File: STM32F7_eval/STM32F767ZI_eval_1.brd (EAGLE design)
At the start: 76.2 x 53.3 mm, 100 parts, among them CN3 GROVE-4P-CONN-I2C-90D, CN4 GROVE-4P-CONN-AN01-90D, CN5 ARDUINO_COMPAT_IF, CN6 STLINKV21_SWD_IF, CN7 WFT0750CZ09-SMD_, CN8 MCO_IF, CN9 UART_IF, Q1 PMF370XN_, SW1 SKRPACE010_, SW2 SKRPACE010_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

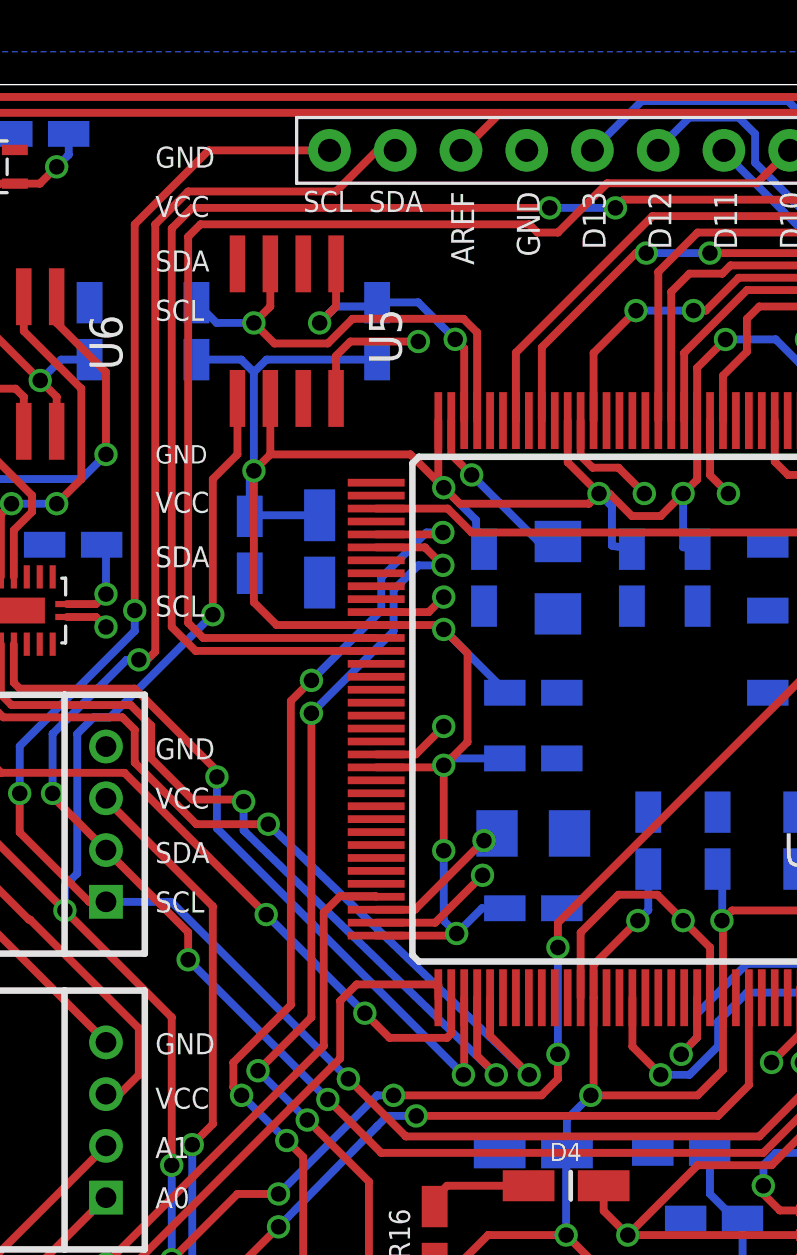
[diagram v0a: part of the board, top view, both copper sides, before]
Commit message: 評価回路を修正
・オプションデバイス電圧とメイン電圧間にジャンパーを挿入
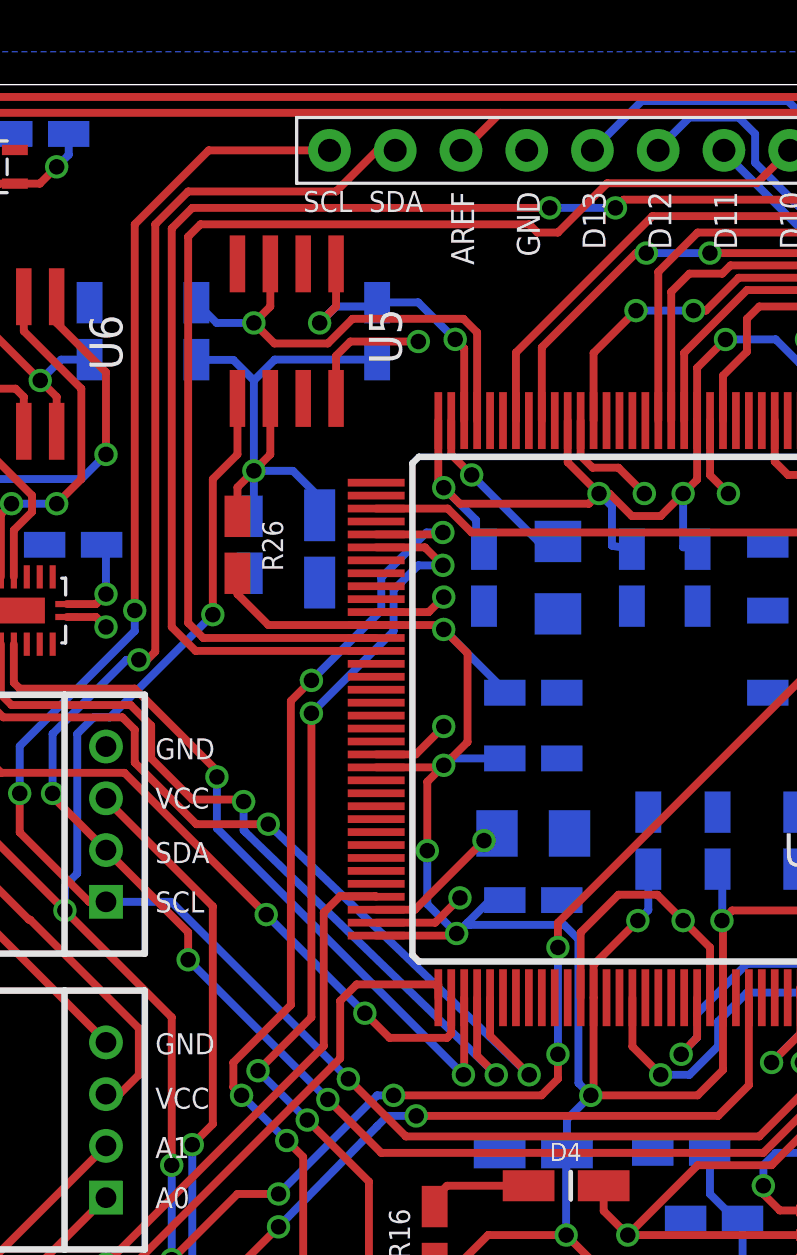
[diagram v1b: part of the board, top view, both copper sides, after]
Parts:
- added R26: 0, Parts:SMD_1608_DEV
- moved C4 0.32 mm to (26.7, 21.8)
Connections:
- new net VCC_STSAFE: C28.1, C29.1, R19.2, R20.2, R26.1, U5.2
- net VDD: now also R26.2; no longer C28.1, C29.1, R19.2, R20.2, U5.2
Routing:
- net VCC_STSAFE: track 0.00 -> 22.1 mm, vias 0 -> 1
- net VDD: track 290.2 -> 272.8 mm, vias 25 -> 24
- net 0V: track 185.7 -> 184.4 mm

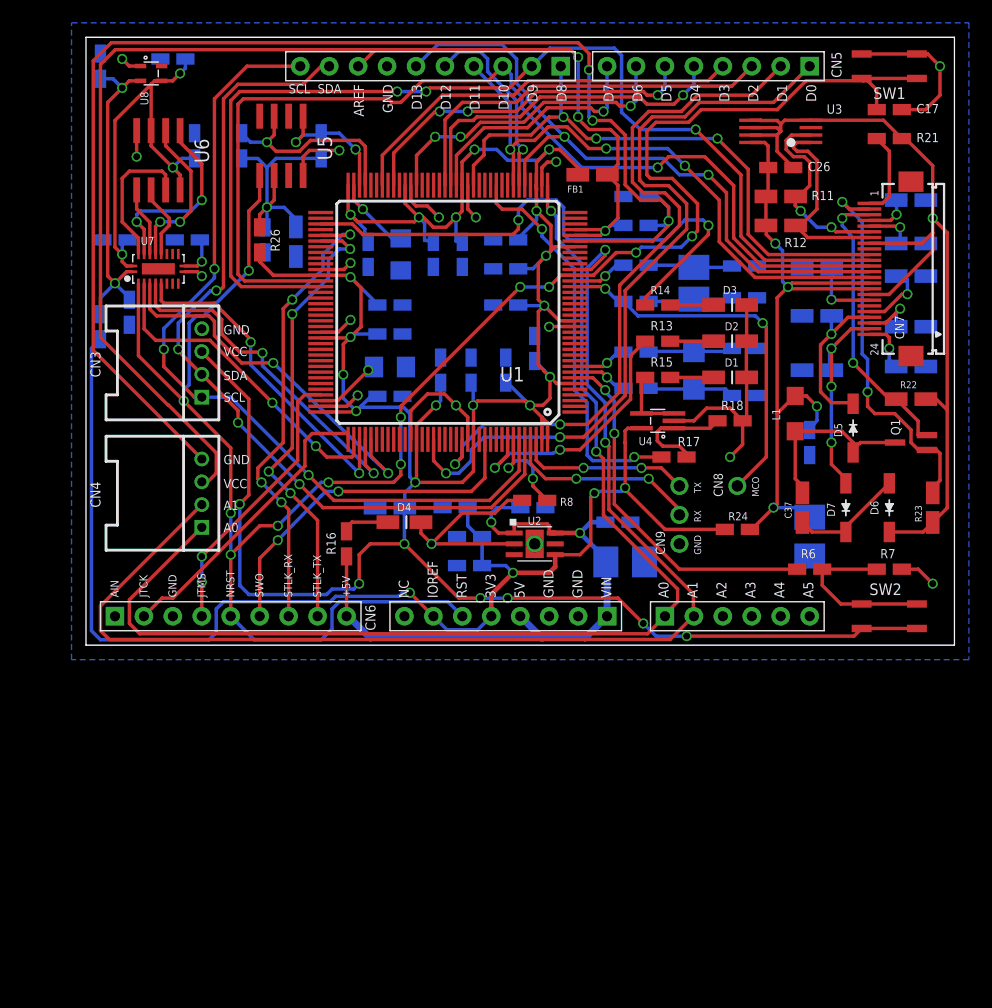
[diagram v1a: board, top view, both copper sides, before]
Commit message: 評価回路を修正
・回り込んだ配線を見直して修正
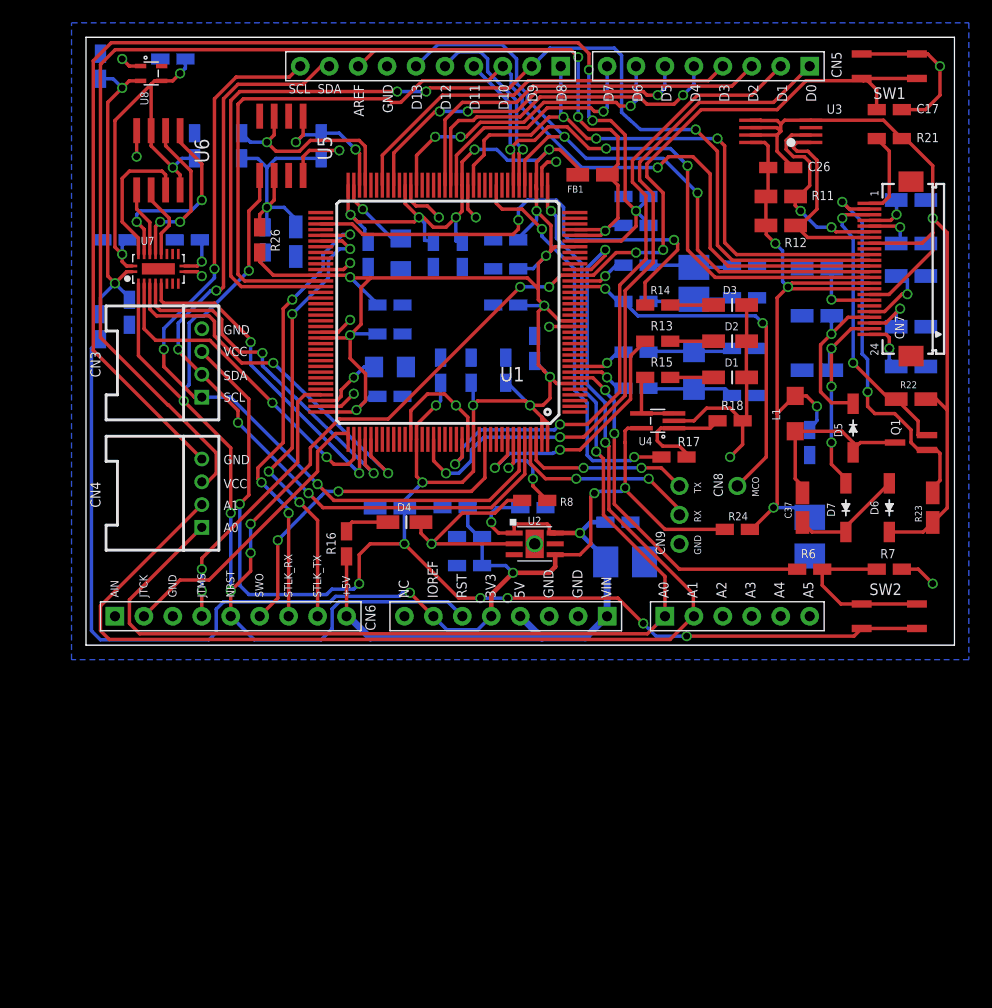
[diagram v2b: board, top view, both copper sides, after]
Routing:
- net AGND: track 117.5 -> 110.6 mm
- net PB14: track 49.7 -> 43.5 mm
- net PG9: track 68.2 -> 62.9 mm
- net PG14: track 63.5 -> 58.2 mm
- net VDD: track 272.8 -> 277.9 mm, vias 24 -> 23
- net NRST: track 176.7 -> 171.6 mm, vias 12 -> 10
- net PA7: track 51.9 -> 54.1 mm
- net PD15: track 95.4 -> 97.1 mm
- net PF12: track 51.9 -> 53.5 mm
- net PD14: track 91.4 -> 92.5 mm
- net PA3: track 102.1 -> 101.1 mm
- net PA15: track 28.5 -> 29.2 mm
- net PA5: track 59.3 -> 59.8 mm

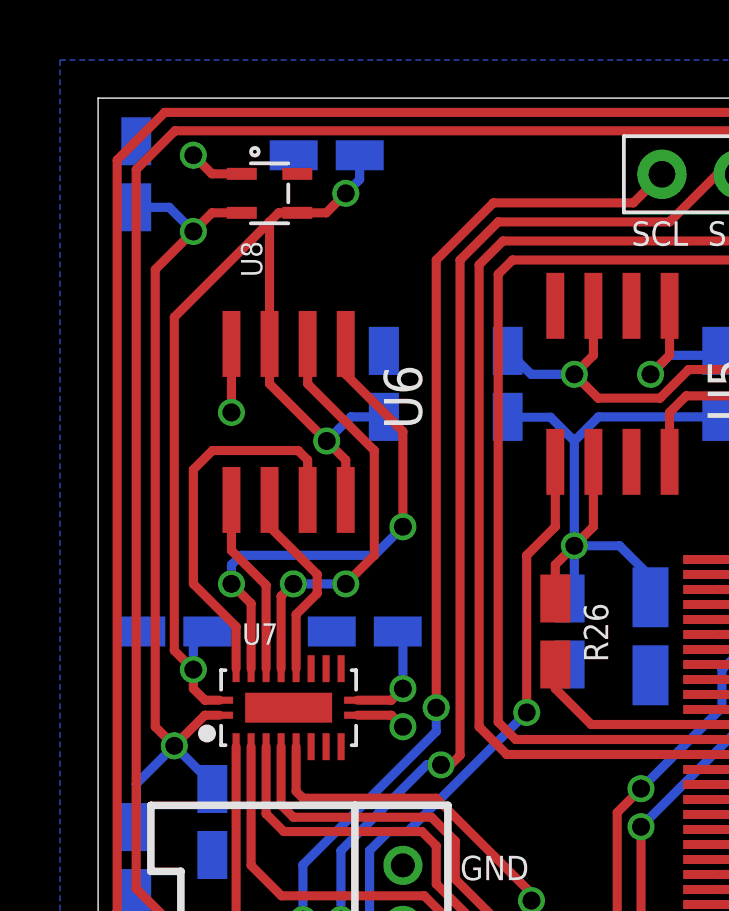
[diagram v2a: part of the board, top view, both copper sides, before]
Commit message: 評価回路を修正
・手はんだパターンに置換え
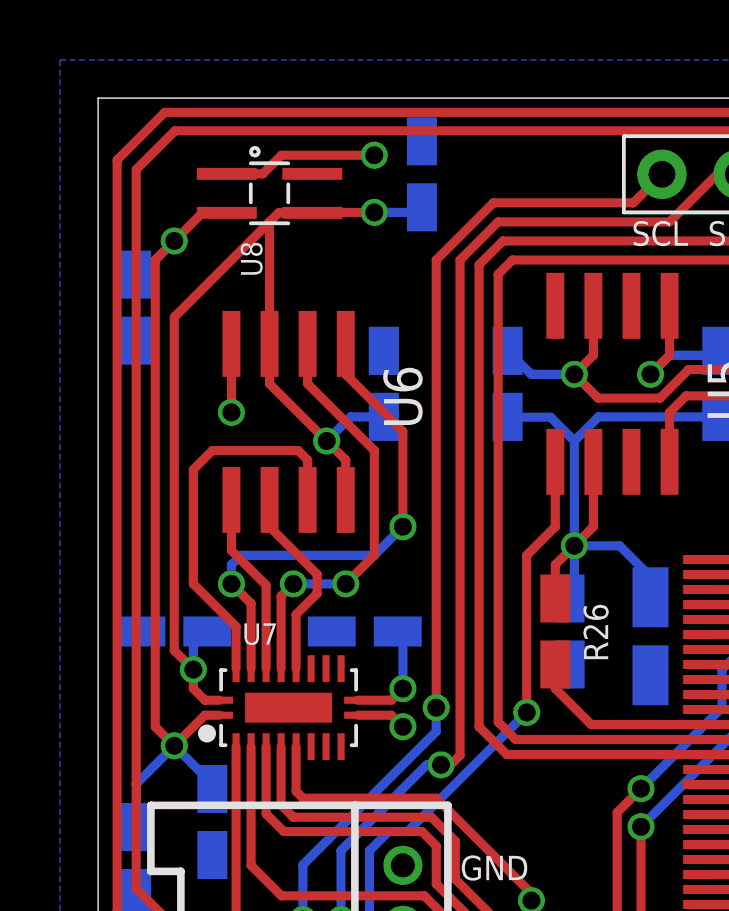
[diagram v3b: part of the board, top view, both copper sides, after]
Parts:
- U8: device Parts:SC-70-4 -> Parts:SC-70-4_DEV
- moved C43 4.45 mm to (1.27, 46.4), turned to 270 degrees
- moved C44 3.24 mm to (10.8, 50.8), turned to 90 degrees
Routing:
- net 0V: track 184.1 -> 187.9 mm
- net +18V: track 36.6 -> 38.0 mm
- net VCC_MEM: track 29.2 -> 28.4 mm
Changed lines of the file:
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@@
 <element name="C42" library="Parts" package="SMD_1608_DEV" value="0.1uF" x="9.525" y="43.815" rot="MR90"/>
 <element name="U7" library="Parts" package="DQFN20" value="FXMA108" x="6.35" y="33.02"/>
-<element name="U8" library="Parts" package="SC-70-4" value="NCP563" x="5.715" y="50.165" smashed="yes" rot="R270">
+<element name="U8" library="Parts" package="SC-70-4_DEV" value="NCP563" x="5.715" y="50.165" smashed="yes" rot="R270">
 <attribute name="NAME" x="4.7625" y="48.5775" size="0.7112" layer="25" rot="R270"/>
 <attribute name="VALUE" x="2.8575" y="51.1175" size="0.7112" layer="27" rot="R270"/>
 </element>
-<element name="C43" library="Parts" package="SMD_1608_DEV" value="1uF" x="1.27" y="50.8" rot="MR90"/>
-<element name="C44" library="Parts" package="SMD_1608_DEV" value="0.1uF" x="7.62" y="51.435" smashed="yes" rot="MR0">
-<attribute name="NAME" x="8.5725" y="52.3875" size="0.8128" layer="26" rot="MR0"/>
-<attribute name="VALUE" x="8.255" y="49.53" size="0.8128" layer="28" rot="MR0"/>
+<element name="C43" library="Parts" package="SMD_1608_DEV" value="1uF" x="1.27" y="46.355" rot="MR270"/>
+<element name="C44" library="Parts" package="SMD_1608_DEV" value="0.1uF" x="10.795" y="50.8" smashed="yes" rot="MR90">
+<attribute name="NAME" x="11.7475" y="49.8475" size="0.8128" layer="26" rot="MR90"/>
+<attribute name="VALUE" x="8.89" y="50.165" size="0.8128" layer="28" rot="MR90"/>
 </element>
 <element name="R5" library="Parts" package="SMD_1608_DEV" value="10k" x="8.89" y="35.56" rot="MR180"/>
@@
 <contactref element="R5" pad="1"/>
 <via x="10.16" y="32.385" extent="1-16" drill="0.6"/>
-<via x="3.175" y="51.435" extent="1-16" drill="0.6"/>
-<wire x1="4.79" y1="50.815" x2="3.795" y2="50.815" width="0.3048" layer="1"/>
-<wire x1="3.795" y1="50.815" x2="3.175" y2="51.435" width="0.3048" layer="1"/>
+<via x="9.2075" y="51.435" extent="1-16" drill="0.6"/>
+<wire x1="4.29" y1="50.815" x2="3.795" y2="50.815" width="0.3048" layer="1"/>
 <via x="4.445" y="42.8625" extent="1-16" drill="0.6"/>
 <wire x1="8.65" y1="32.77" x2="9.775" y2="32.77" width="0.3048" layer="1"/>
@@
 <wire x1="20.6" y1="20.96" x2="22.38875" y2="20.96" width="0.3048" layer="1"/>
 <wire x1="22.38875" y1="20.96" x2="23.495" y2="22.06625" width="0.3048" layer="1"/>
+<wire x1="4.29" y1="50.815" x2="5.491875" y2="50.815" width="0.3048" layer="1"/>
+<wire x1="5.491875" y1="50.815" x2="6.111875" y2="51.435" width="0.3048" layer="1"/>
+<wire x1="6.111875" y1="51.435" x2="9.2075" y2="51.435" width="0.3048" layer="1"/>
 </signal>
 <signal name="N$2">
@@
 <via x="3.175" y="34.29" extent="1-16" drill="0.6"/>
 <via x="7.62" y="41.91" extent="1-16" drill="0.6"/>
-<via x="8.255" y="50.165" extent="1-16" drill="0.6"/>
+<via x="9.2075" y="49.53" extent="1-16" drill="0.6"/>
 <wire x1="3.175" y1="34.29" x2="2.54" y2="34.925" width="0.3048" layer="1"/>
 <wire x1="2.54" y1="34.925" x2="2.54" y2="46.0375" width="0.3048" layer="1"/>
@@
 <wire x1="3.56" y1="33.27" x2="3.175" y2="33.655" width="0.3048" layer="1"/>
 <wire x1="3.175" y1="33.655" x2="3.175" y2="34.29" width="0.3048" layer="1"/>
-<wire x1="6.64" y1="49.515" x2="6.0175" y2="49.515" width="0.3048" layer="1"/>
+<wire x1="7.14" y1="49.515" x2="6.0175" y2="49.515" width="0.3048" layer="1"/>
 <wire x1="2.54" y1="46.0375" x2="5.715" y2="49.2125" width="0.3048" layer="1"/>
-<wire x1="6.64" y1="49.515" x2="7.605" y2="49.515" width="0.3048" layer="1"/>
-<wire x1="7.605" y1="49.515" x2="8.255" y2="50.165" width="0.3048" layer="1"/>
-<wire x1="8.72" y1="51.435" x2="8.72" y2="50.63" width="0.3048" layer="16"/>
-<wire x1="8.72" y1="50.63" x2="8.255" y2="50.165" width="0.3048" layer="16"/>
+<wire x1="7.14" y1="49.515" x2="7.605" y2="49.515" width="0.3048" layer="1"/>
 <wire x1="8.255" y1="39.945" x2="8.255" y2="41.275" width="0.3048" layer="1"/>
 <wire x1="8.255" y1="41.275" x2="7.62" y2="41.91" width="0.3048" layer="1"/>
@@
 <wire x1="3.175" y1="34.29" x2="3.175" y2="35.095" width="0.3048" layer="16"/>
 <wire x1="3.175" y1="35.095" x2="3.64" y2="35.56" width="0.3048" layer="16"/>
+<wire x1="9.2075" y1="49.53" x2="10.795" y2="49.53" width="0.3048" layer="16"/>
+<wire x1="10.795" y1="49.53" x2="10.795" y2="49.7" width="0.3048" layer="16"/>
+<wire x1="9.2075" y1="49.53" x2="7.14" y2="49.53" width="0.3048" layer="1"/>
+<wire x1="7.14" y1="49.53" x2="7.14" y2="49.515" width="0.3048" layer="1"/>
 </signal>
 <signal name="!RESET!">
@@
 <contactref element="R25" pad="2"/>
 <via x="2.54" y="31.75" extent="1-16" drill="0.6"/>
-<via x="3.175" y="48.895" extent="1-16" drill="0.6"/>
-<wire x1="1.905" y1="47.625" x2="1.905" y2="32.385" width="0.3048" layer="1"/>
+<via x="2.54" y="48.5775" extent="1-16" drill="0.6"/>
+<wire x1="1.905" y1="47.9425" x2="1.905" y2="32.385" width="0.3048" layer="1"/>
 <wire x1="1.905" y1="32.385" x2="2.54" y2="31.75" width="0.3048" layer="1"/>
 <wire x1="1.27" y1="29.04" x2="1.27" y2="30.48" width="0.3048" layer="16"/>
@@
 <wire x1="4.05" y1="32.77" x2="3.56" y2="32.77" width="0.3048" layer="1"/>
 <wire x1="3.56" y1="32.77" x2="2.54" y2="31.75" width="0.3048" layer="1"/>
-<wire x1="3.175" y1="48.895" x2="1.905" y2="47.625" width="0.3048" layer="1"/>
-<wire x1="4.79" y1="49.515" x2="3.795" y2="49.515" width="0.3048" layer="1"/>
-<wire x1="3.795" y1="49.515" x2="3.175" y2="48.895" width="0.3048" layer="1"/>
-<wire x1="1.27" y1="49.7" x2="2.37" y2="49.7" width="0.3048" layer="16"/>
-<wire x1="2.37" y1="49.7" x2="3.175" y2="48.895" width="0.3048" layer="16"/>
+<wire x1="4.29" y1="49.515" x2="3.4775" y2="49.515" width="0.3048" layer="1"/>
 <wire x1="3.81" y1="30.31" x2="3.81" y2="30.48" width="0.3048" layer="16"/>
 <wire x1="3.81" y1="30.48" x2="2.54" y2="31.75" width="0.3048" layer="16"/>
+<wire x1="1.905" y1="47.9425" x2="2.54" y2="48.5775" width="0.3048" layer="1"/>
+<wire x1="2.54" y1="48.5775" x2="3.4775" y2="49.515" width="0.3048" layer="1"/>
+<wire x1="1.27" y1="47.455" x2="1.4175" y2="47.455" width="0.3048" layer="16"/>
+<wire x1="1.4175" y1="47.455" x2="2.54" y2="48.5775" width="0.3048" layer="16"/>
 </signal>
 <signal name="N$15">

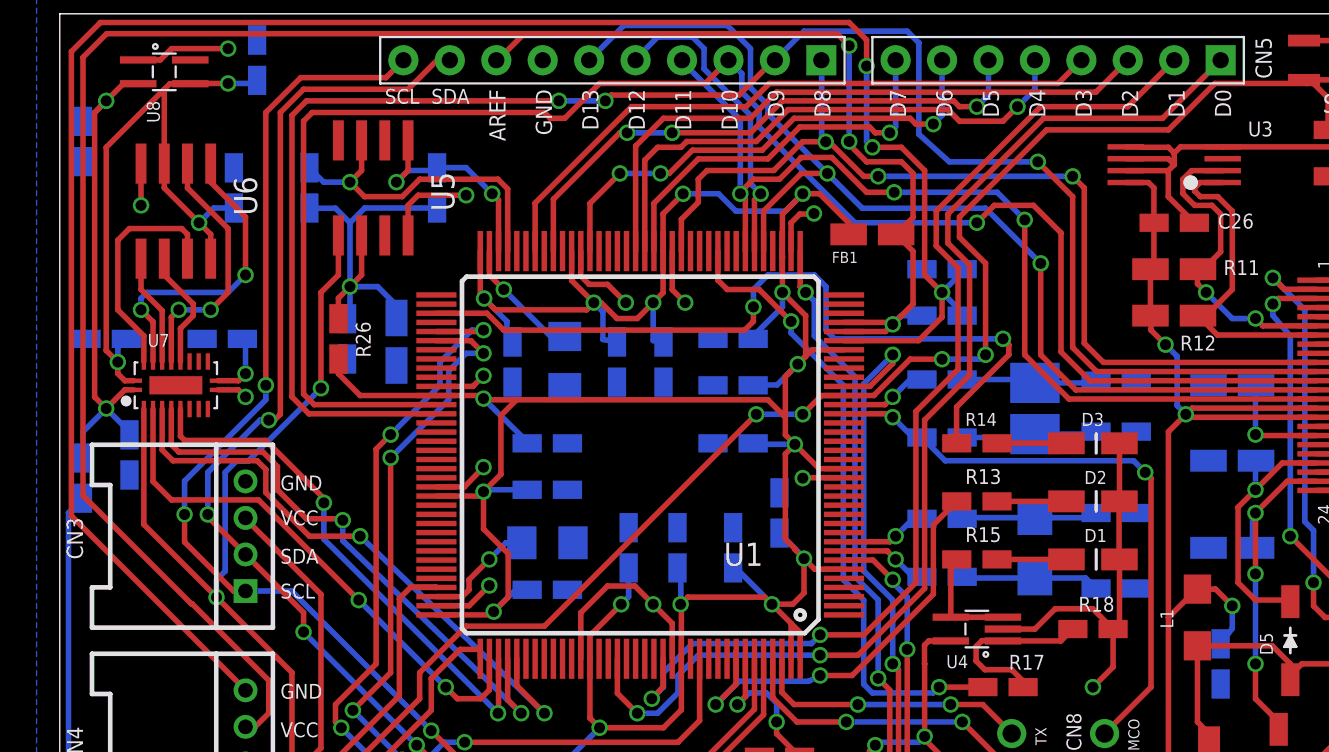
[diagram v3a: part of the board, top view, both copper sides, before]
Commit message: 評価回路を修正
・手はんだパターンに置換え
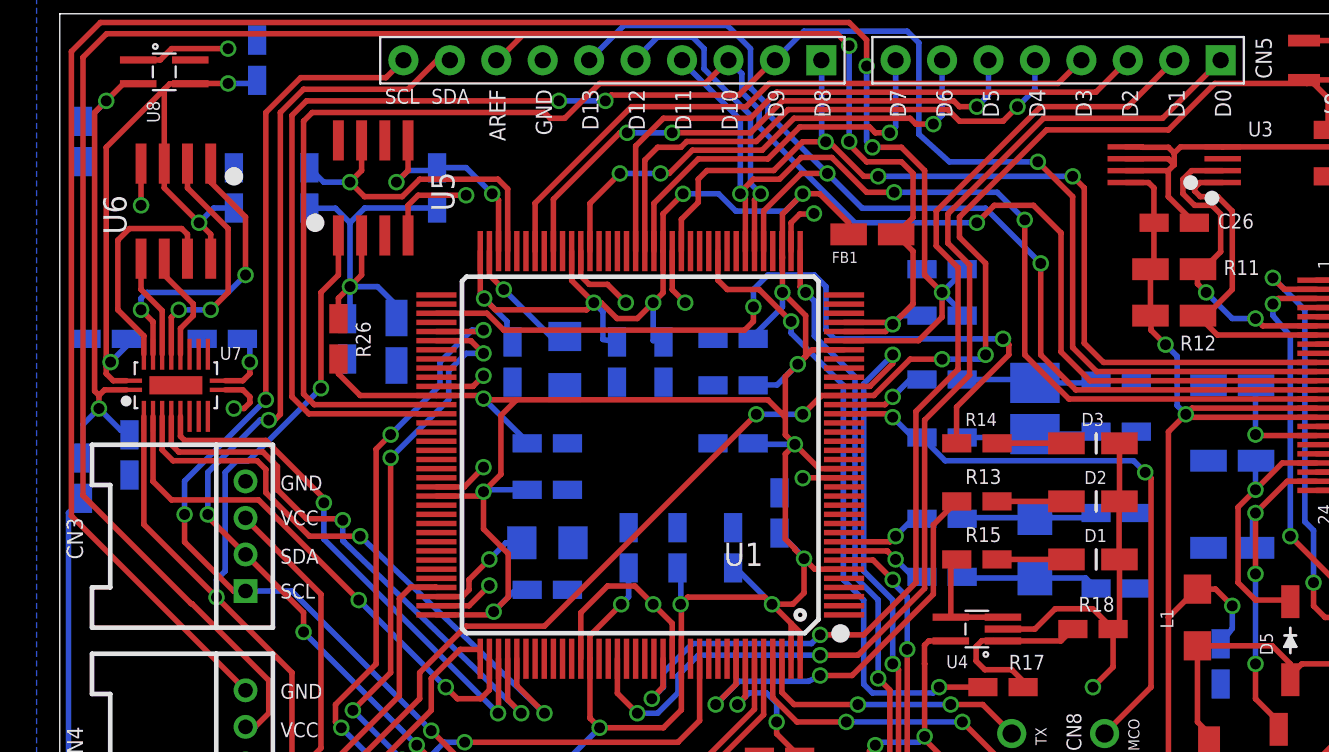
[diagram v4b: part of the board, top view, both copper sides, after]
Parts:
- U7: value FXMA108 -> FXMA108_; device Parts:DQFN20 -> Parts:DQFN20_DEV
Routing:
- net 0V: track 187.9 -> 189.1 mm
